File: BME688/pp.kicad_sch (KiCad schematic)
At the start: 12 parts, among them J1 Conn_01x03, J2 Conn_01x04, U1 BME688, U2 CH32V003AxMx, U3 AP62250WU-7

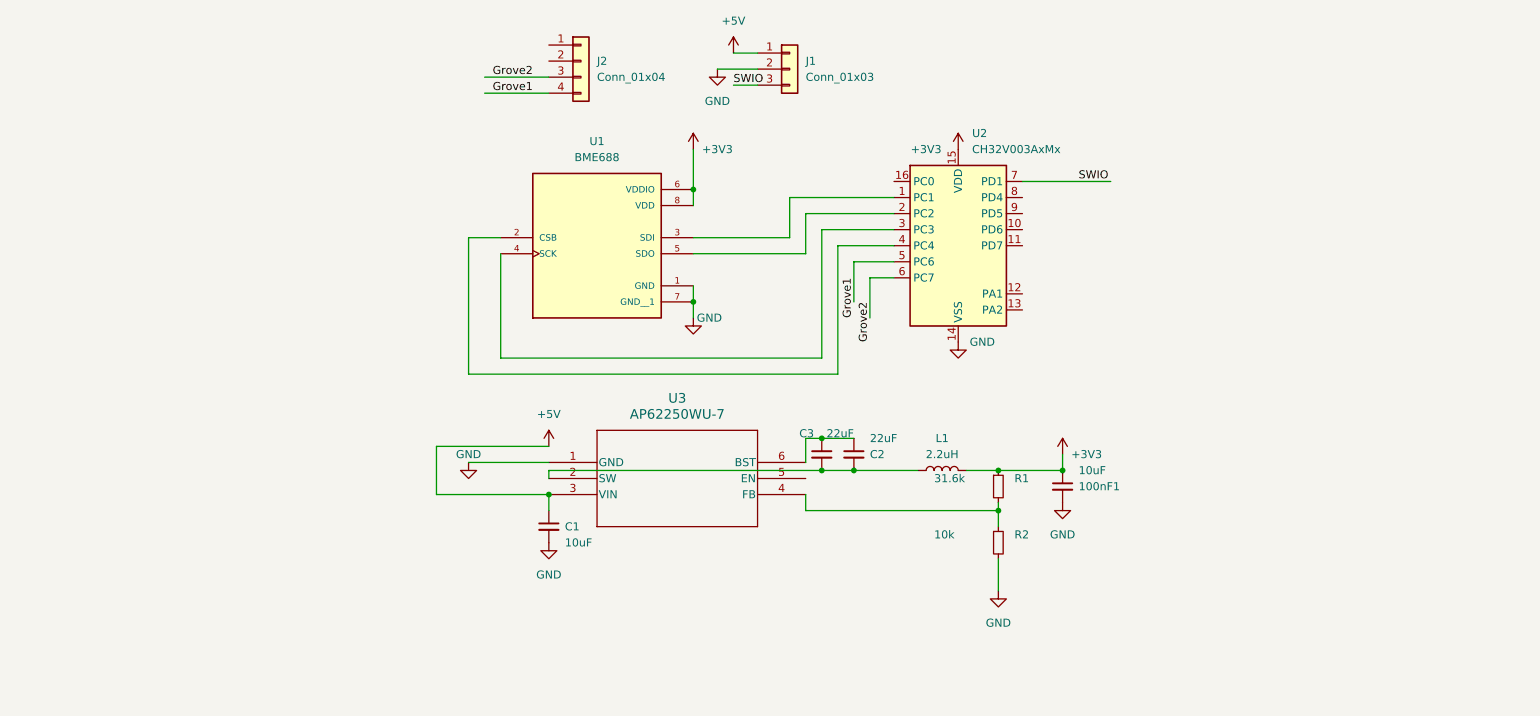
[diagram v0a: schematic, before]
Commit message: Swap over to STM32 controller
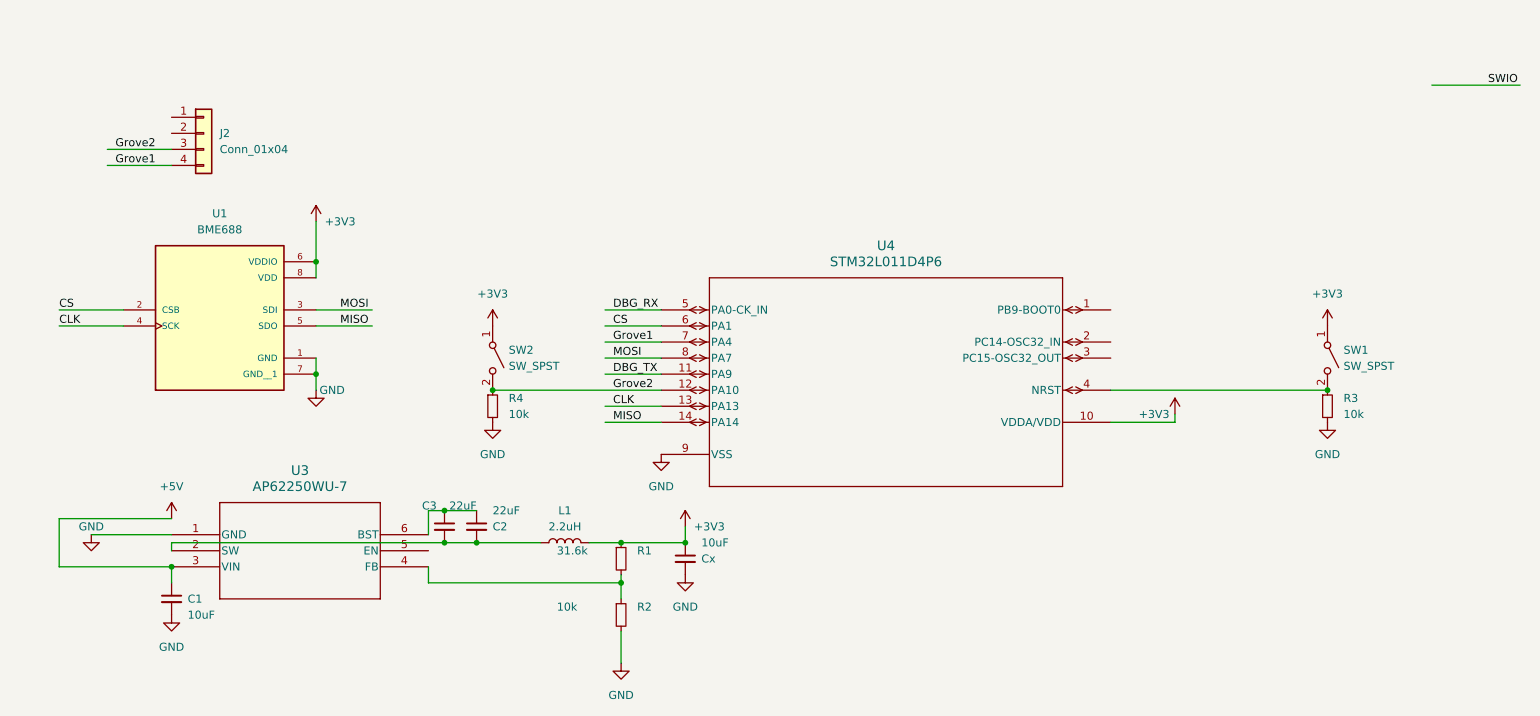
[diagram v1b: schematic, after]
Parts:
- removed J1: Conn_01x03, Connector_JST:JST_EH_B3B-EH-A_1x03_P2.50mm_Vertical, symbol Connector_Generic:Conn_01x03
- removed U2: CH32V003AxMx, Package_SO:SOP-16_3.9x9.9mm_P1.27mm, symbol MCU_WCH_CH32V0:CH32V003AxMx
- added R3, R4: 10k, Resistor_SMD:R_0805_2012Metric, symbol Device:R_Small
- added SW1, SW2: SW_SPST, Jumper:SolderJumper-2_P1.3mm_Open_TrianglePad1.0x1.5mm, symbol Switch:SW_SPST
- added U4: STM32L011D4P6, DOcuments folder:TSSOP14, symbol STM32:STM32L011D4P7
- renumbered 100nF1 to Cx
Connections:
- net +3V3: now also SW1.1 (A), SW2.1 (A), U4.10 (VDDA/VDD)
- net GND: now also R3.2, R4.2, U4.9 (VSS)
- net Grove1: now also U4.7 (PA4)
- net Grove2: now also R4.1, SW2.2 (B), U4.12 (PA10)
- net CS: now reaches U1.2 (CSB)
- net CS: now also U4.6 (PA1)
- net MOSI: now reaches U1.3 (SDI)
- net MOSI: now also U4.8 (PA7)
- net CLK: now reaches U1.4 (SCK)
- net CLK: now also U4.13 (PA13)
- net MISO: now reaches U1.5 (SDO)
- net MISO: now also U4.14 (PA14)
- new net: R3.1, SW1.2 (B), U4.4 (NRST)
- new net DBG_RX: U4.5 (PA0-CK_IN)
- new net DBG_TX: U4.11 (PA9)
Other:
- moved on the sheet: C1, C2, C3, Cx, J2, L1, R1, R2, U1, U3

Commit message: Migrate to STM32
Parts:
- added R5: 10k, Resistor_SMD:R_0402_1005Metric, symbol Device:R
- renumbered Cx to Cx1
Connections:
- net +3V3: now also R5.1
- net CS: now also R5.2
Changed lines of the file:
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@@
 	(paper "A4")
+	(junction
+		(at 50.8 105.41)
+		(diameter 0)
+		(color 0 0 0 0)
+	)
 	(junction
 		(at 144.78 142.24)
@@
 	(wire
 		(pts
-			(xy 45.72 105.41) (xy 55.88 105.41)
-		)
-		(stroke
-			(width 0)
-			(type default)
-		)
-	)
-	(wire
-		(pts
 			(xy 104.14 140.97) (xy 104.14 137.16)
 		)
@@
 	(wire
 		(pts
+			(xy 45.72 105.41) (xy 50.8 105.41)
+		)
+		(stroke
+			(width 0)
+			(type default)
+		)
+	)
+	(wire
+		(pts
 			(xy 144.78 139.7) (xy 144.78 142.24)
 		)
@@
 		(pts
 			(xy 63.5 138.43) (xy 45.72 138.43)
+		)
+		(stroke
+			(width 0)
+			(type default)
+		)
+	)
+	(wire
+		(pts
+			(xy 50.8 105.41) (xy 55.88 105.41)
 		)
 		(stroke
@@
 		(on_board yes)
 		(dnp no)
-		(property "Reference" "Cx"
+		(property "Reference" "Cx1"
 			(at 147.32 144.78 0)
 			(effects
@@
 			(project "pp"
 				(path "/26f2ad55-1934-4bdb-b946-cbdd01bda2f2"
-					(reference "Cx")
+					(reference "Cx1")
 					(unit 1)
 				)
@@
 				(path "/26f2ad55-1934-4bdb-b946-cbdd01bda2f2"
 					(reference "R3")
+					(unit 1)
+				)
+			)
+		)
+	)
+	(symbol
+		(lib_id "Device:R")
+		(at 50.8 101.6 0)
+		(unit 1)
+		(exclude_from_sim no)
+		(in_bom yes)
+		(on_board yes)
+		(dnp no)
+		(fields_autoplaced yes)
+		(property "Reference" "R5"
+			(at 53.34 100.3299 0)
+			(effects
+				(font
+					(size 1.27 1.27)
+				)
+				(justify left)
+			)
+		)
+		(property "Value" "10k"
+			(at 53.34 102.8699 0)
+			(effects
+				(font
+					(size 1.27 1.27)
+				)
+				(justify left)
+			)
+		)
+		(property "Footprint" "Resistor_SMD:R_0402_1005Metric"
+			(at 49.022 101.6 90)
+			(effects
+				(font
+					(size 1.27 1.27)
+				)
+				(hide yes)
+			)
+		)
+		(property "Datasheet" "~"
+			(at 50.8 101.6 0)
+			(effects
+				(font
+					(size 1.27 1.27)
+				)
+				(hide yes)
+			)
+		)
+		(property "Description" "Resistor"
+			(at 50.8 101.6 0)
+			(effects
+				(font
+					(size 1.27 1.27)
+				)
+				(hide yes)
+			)
+		)
+		(pin "1"
+		)
+		(pin "2"
+		)
+		(instances
+			(project ""
+				(path "/26f2ad55-1934-4bdb-b946-cbdd01bda2f2"
+					(reference "R5")
 					(unit 1)
 				)
@@
 					(unit 1)
 				)
+			)
+		)
+	)
+	(symbol
+		(lib_name "+3V3_3")
+		(lib_id "power:+3V3")
+		(at 50.8 97.79 0)
+		(unit 1)
+		(exclude_from_sim no)
+		(in_bom yes)
+		(on_board yes)
+		(dnp no)
+		(fields_autoplaced yes)
+		(property "Reference" "#PWR05"
+			(at 50.8 101.6 0)
+			(effects
+				(font
+					(size 1.27 1.27)
+				)
+				(hide yes)
+			)
+		)
+		(property "Value" "+3V3"
+			(at 50.8 92.71 0)
+			(effects
+				(font
+					(size 1.27 1.27)
+				)
+			)
+		)
+		(property "Footprint" ""
+			(at 50.8 97.79 0)
+			(effects
+				(font
+					(size 1.27 1.27)
+				)
+				(hide yes)
+			)
+		)
+		(property "Datasheet" ""
+			(at 50.8 97.79 0)
+			(effects
+				(font
+					(size 1.27 1.27)
+				)
+				(hide yes)
+			)
+		)
+		(property "Description" "Power symbol creates a global label with name \"+3V3\""
+			(at 50.8 97.79 0)
+			(effects
+				(font
+					(size 1.27 1.27)
+				)
+				(hide yes)
+			)
+		)
+		(pin "1"
+		)
+		(instances
+			(project ""
+				(path "/26f2ad55-1934-4bdb-b946-cbdd01bda2f2"
+					(reference "#PWR05")
+					(unit 1)
+				)

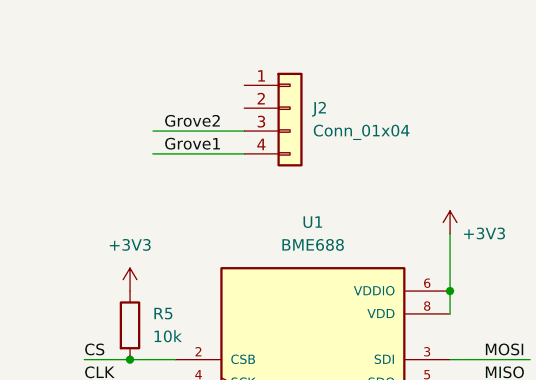
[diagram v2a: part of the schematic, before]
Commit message: Fix power on BME grove port
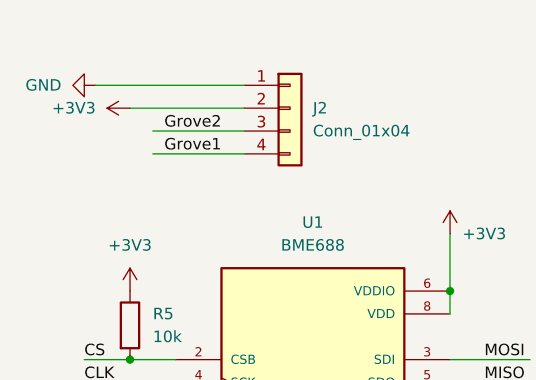
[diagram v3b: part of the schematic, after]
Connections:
- net +3V3: now also J2.2 (Pin_2)
- net GND: now also J2.1 (Pin_1)
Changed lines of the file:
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@@
+	(wire
+		(pts
+			(xy 50.8 77.47) (xy 63.5 77.47)
+		)
+		(stroke
+			(width 0)
+			(type default)
+		)
+	)
 	(wire
 		(pts
@@
 		(pts
 			(xy 114.3 118.11) (xy 140.97 118.11)
+		)
+		(stroke
+			(width 0)
+			(type default)
+		)
+	)
+	(wire
+		(pts
+			(xy 46.99 74.93) (xy 63.5 74.93)
 		)
 		(stroke
@@
 	)
 	(symbol
+		(lib_id "power:VCC")
+		(at 50.8 77.47 90)
+		(unit 1)
+		(exclude_from_sim no)
+		(in_bom yes)
+		(on_board yes)
+		(dnp no)
+		(fields_autoplaced yes)
+		(property "Reference" "#PWR06"
+			(at 54.61 77.47 0)
+			(effects
+				(font
+					(size 1.27 1.27)
+				)
+				(hide yes)
+			)
+		)
+		(property "Value" "+3V3"
+			(at 46.99 77.4699 90)
+			(effects
+				(font
+					(size 1.27 1.27)
+				)
+				(justify left)
+			)
+		)
+		(property "Footprint" ""
+			(at 50.8 77.47 0)
+			(effects
+				(font
+					(size 1.27 1.27)
+				)
+				(hide yes)
+			)
+		)
+		(property "Datasheet" ""
+			(at 50.8 77.47 0)
+			(effects
+				(font
+					(size 1.27 1.27)
+				)
+				(hide yes)
+			)
+		)
+		(property "Description" "Power symbol creates a global label with name \"VCC\""
+			(at 50.8 77.47 0)
+			(effects
+				(font
+					(size 1.27 1.27)
+				)
+				(hide yes)
+			)
+		)
+		(pin "1"
+		)
+		(instances
+			(project ""
+				(path "/26f2ad55-1934-4bdb-b946-cbdd01bda2f2"
+					(reference "#PWR06")
+					(unit 1)
+				)
+			)
+		)
+	)
+	(symbol
 		(lib_id "Device:C_Small")
 		(at 144.78 144.78 0)
@@
 					(unit 1)
 				)
+			)
+		)
+	)
+	(symbol
+		(lib_name "GND_3")
+		(lib_id "power:GND")
+		(at 46.99 74.93 270)
+		(unit 1)
+		(exclude_from_sim no)
+		(in_bom yes)
+		(on_board yes)
+		(dnp no)
+		(fields_autoplaced yes)
+		(property "Reference" "#PWR017"
+			(at 40.64 74.93 0)
+			(effects
+				(font
+					(size 1.27 1.27)
+				)
+				(hide yes)
+			)
+		)
+		(property "Value" "GND"
+			(at 43.18 74.9299 90)
+			(effects
+				(font
+					(size 1.27 1.27)
+				)
+				(justify right)
+			)
+		)
+		(property "Footprint" ""
+			(at 46.99 74.93 0)
+			(effects
+				(font
+					(size 1.27 1.27)
+				)
+				(hide yes)
+			)
+		)
+		(property "Datasheet" ""
+			(at 46.99 74.93 0)
+			(effects
+				(font
+					(size 1.27 1.27)
+				)
+				(hide yes)
+			)
+		)
+		(property "Description" "Power symbol creates a global label with name \"GND\" , ground"
+			(at 46.99 74.93 0)
+			(effects
+				(font
+					(size 1.27 1.27)
+				)
+				(hide yes)
+			)
+		)
+		(pin "1"
+		)
+		(instances
+			(project ""
+				(path "/26f2ad55-1934-4bdb-b946-cbdd01bda2f2"
+					(reference "#PWR017")
+					(unit 1)
+				)
